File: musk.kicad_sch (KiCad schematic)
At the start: 53 parts, among them J1 debug-port, J10 bridge, J3 bridge, J4 bridge, J5 bridge, J6 bridge, J7 bridge, J8 bridge, J9 bridge, K1 diode-choc, K10 diode-choc, K11 diode-choc, K12 diode-choc, K13 diode-choc, K14 diode-choc, K15 diode-choc, K16 diode-choc, K17 diode-choc, K2 diode-choc, K3 diode-choc, K4 diode-choc, K5 diode-choc, K6 diode-choc, K7 diode-choc, K8 diode-choc, K9 diode-choc, SW1 SW_Push, SW2 RotaryEncoder, U1 W25Q128, U2 ms88sf3-nrf52840, U3 LSM6DS3, U8 PMW3610

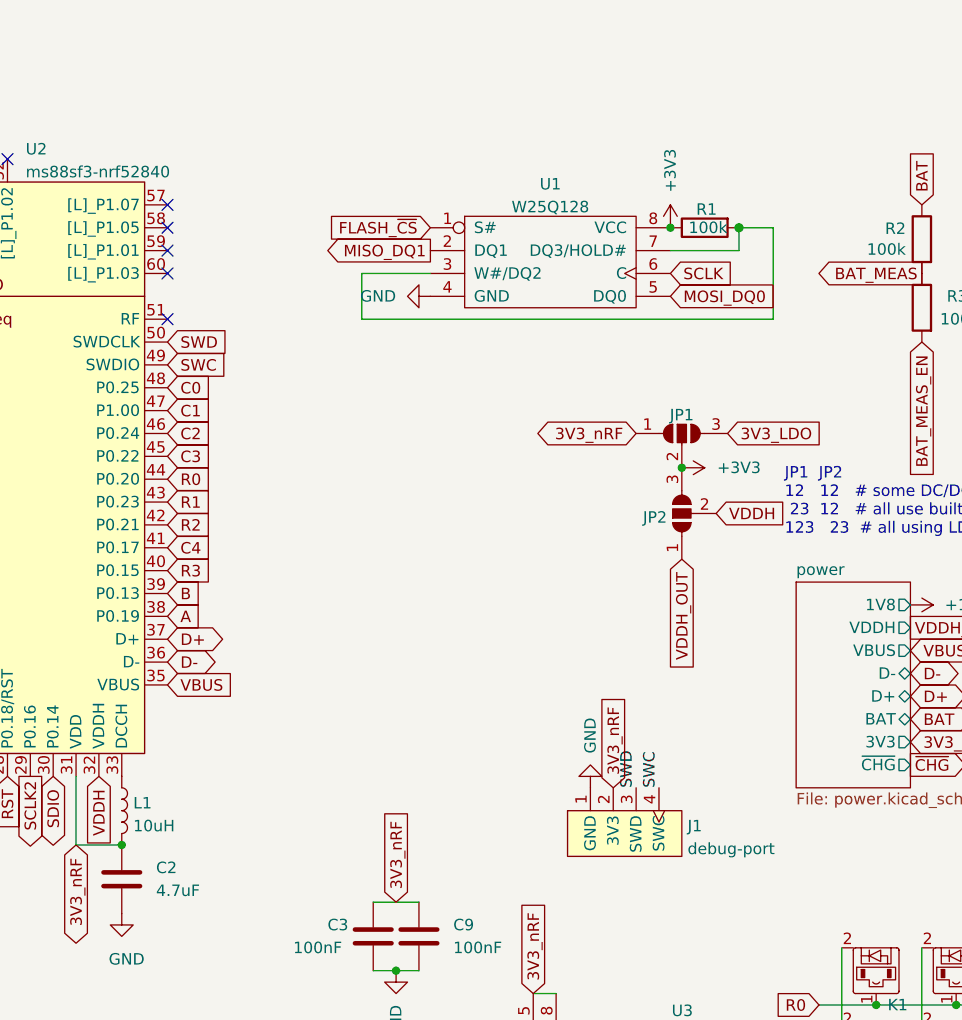
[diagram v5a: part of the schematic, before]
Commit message: add groove for nOOd
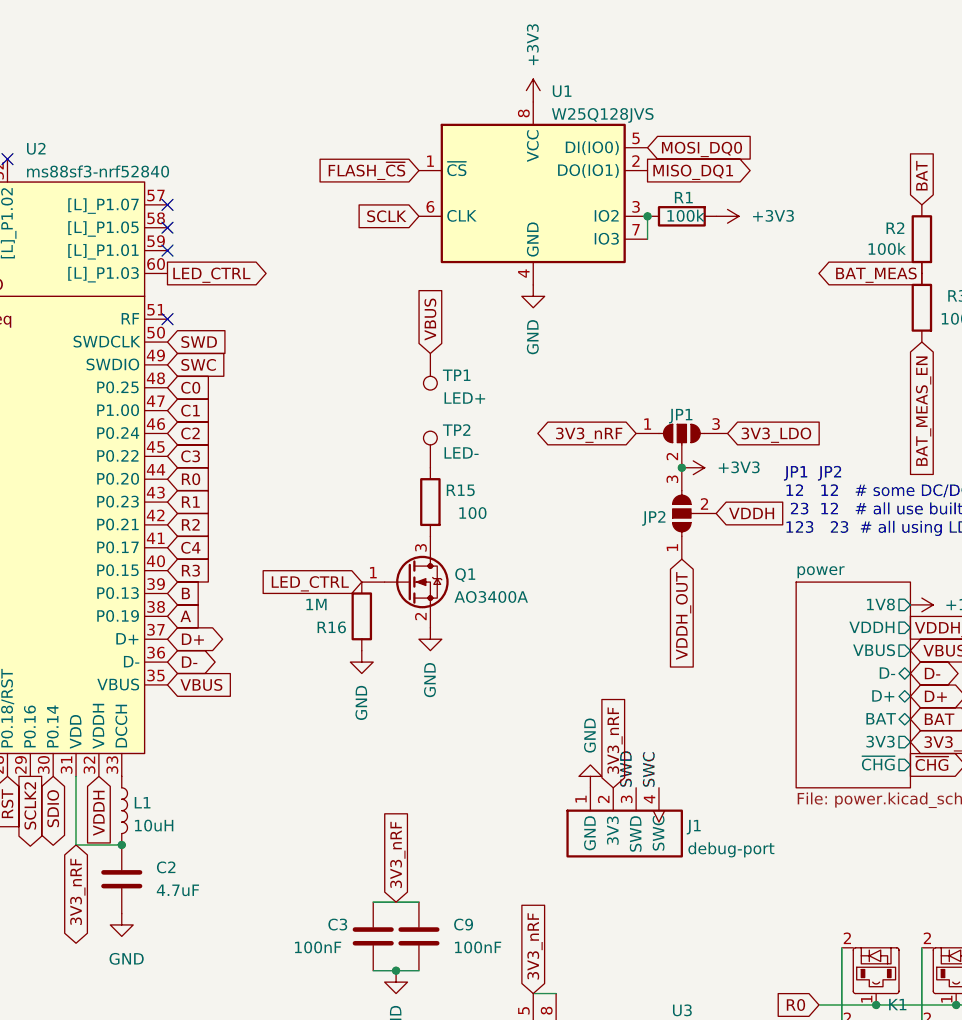
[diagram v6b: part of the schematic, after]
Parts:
- removed U1: W25Q128, Package_SO:SOIC-8_5.23x5.23mm_P1.27mm, symbol ic:MT25QL128ABA1ESE
- added Q1: AO3400A, Package_TO_SOT_SMD:SOT-23, symbol Transistor_FET:AO3400A
- added R15: 100, Resistor_SMD:R_0603_1608Metric, symbol Device:R
- added R16: 1M, Resistor_SMD:R_0603_1608Metric, symbol Device:R
- added TP1: LED+, TestPoint:TestPoint_THTPad_D2.0mm_Drill1.0mm, symbol Connector:TestPoint
- added TP2: LED-, TestPoint:TestPoint_THTPad_D2.0mm_Drill1.0mm, symbol Connector:TestPoint
- added U1: W25Q128JVS, Package_SO:SOIC-8_5.23x5.23mm_P1.27mm, symbol Memory_Flash:W25Q128JVS
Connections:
- net +3V3: now also R1.2, U1.8 (VCC); no longer R1.1
- net FLASH_~{CS}: now also U1.1 (~{CS})
- net GND: now also Q1.2 (S), R16.1, U1.4 (GND)
- net MISO_DQ1: now also U1.2 (DO(IO1))
- net MOSI_DQ0: now also U1.5 (DI(IO0))
- net SCLK: now also U1.6 (CLK)
- net VBUS: now also TP1.1
- net LED_CTRL: now reaches U2.60 ([L]_P1.03)
- net LED_CTRL: now also Q1.1 (G), R16.2
- new net: Q1.3 (D), R15.2
- new net: R15.1, TP2.1
- new net: R1.1, U1.3 (IO2), U1.7 (IO3)
- no-connect marks 25 -> 24
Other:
- moved on the sheet: R1
